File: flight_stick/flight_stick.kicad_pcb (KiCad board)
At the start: 2 copper layers, 75 x 50 mm, 61 parts, among them J10 USB_C_Receptacle_USB2.0, J11 Conn_01x05_Pin, J7 Conn_01x04_Male, J8 Conn_01x05_Pin, J9 Conn_ST_STDC14, Q4 2N7002, Q5 2N7002, Q6 2N7002, Q7 2N7002, Q8 2N7002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

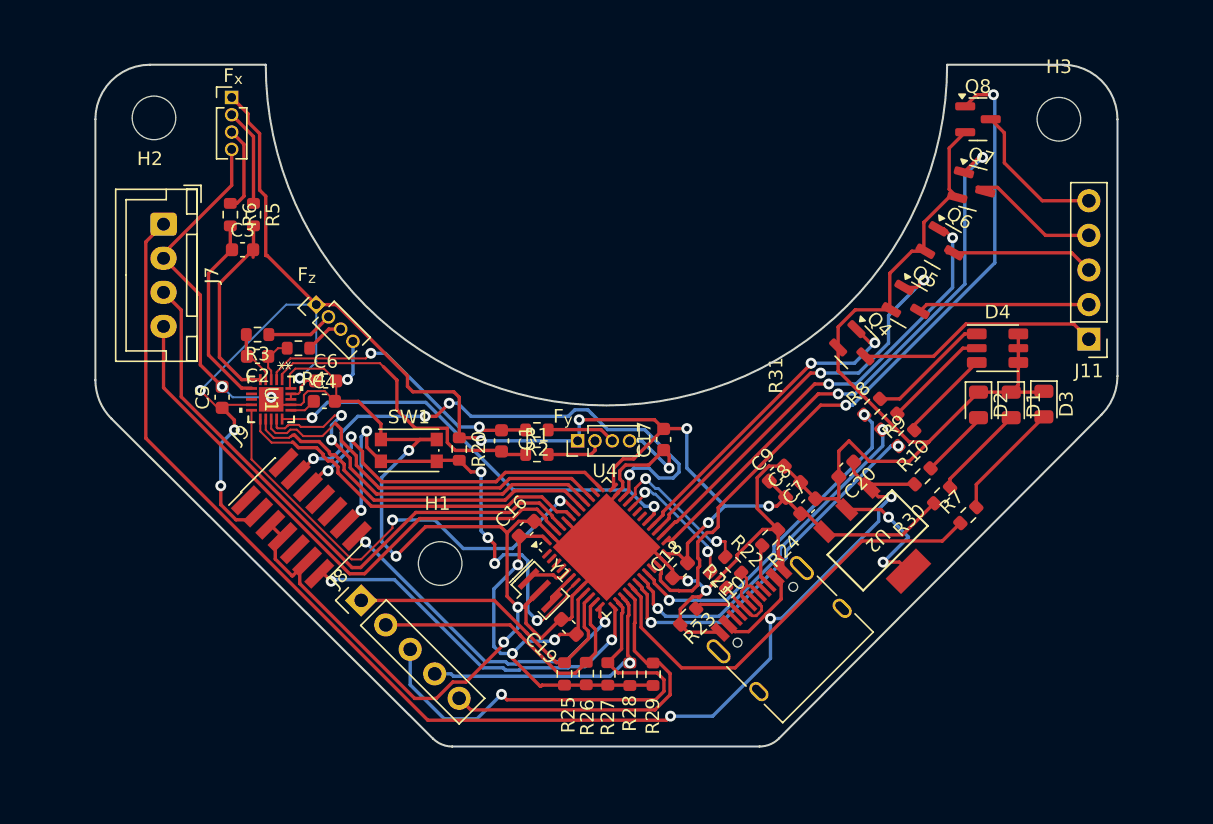
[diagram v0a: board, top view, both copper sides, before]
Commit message: Touchups
- Added GND pour on top
- Cleaned up some traces
- Fixed 3V3 missing connections
- Reduced pad size on ADC for clearance
- Removed last vias in pads
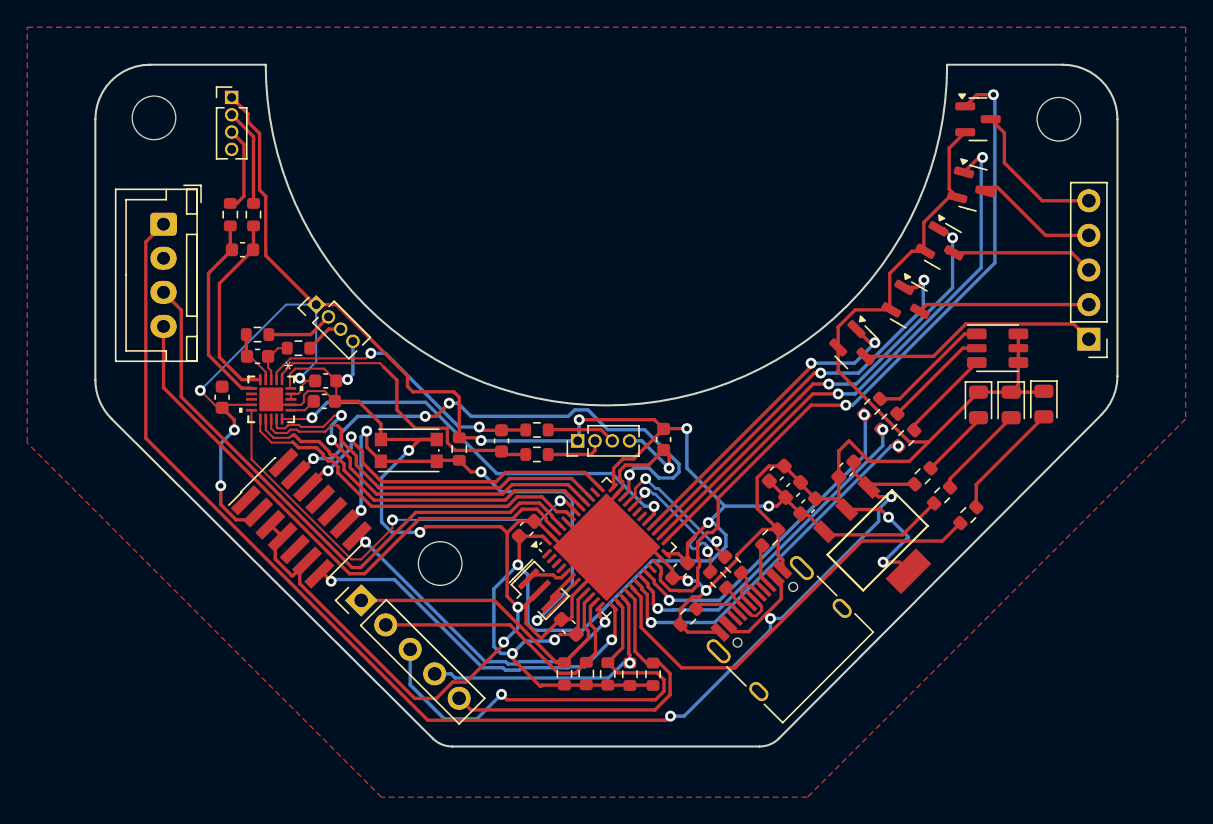
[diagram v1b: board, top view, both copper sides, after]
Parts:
- renumbered F_{y} to J1, F_{z} to J3, F_{x} to J5
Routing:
- net GND: track 261.4 -> 234.0 mm, vias 12 -> 10
- net +3.3V: track 162.4 -> 186.8 mm
- net /mcureset: track 36.9 -> 39.6 mm, vias 6 -> 4
- net /ADC_CS: track 34.6 -> 32.9 mm
- net /D-: track 9.79 -> 11.1 mm
- net +5V: track 103.6 -> 102.4 mm
- net /StatusLED_{B}: track 25.2 -> 24.5 mm
- net /StatusLED_{R}: track 26.1 -> 25.5 mm
- net Net-(U1-AIN2P): track 14.9 -> 14.3 mm
- added copper zone on F.Cu, net GND

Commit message: Updated Layout, Added Assembly part #s
Cleaned up layout for assembly minimum spacing

Added JLCPCB part #s for preorder and manufacturing
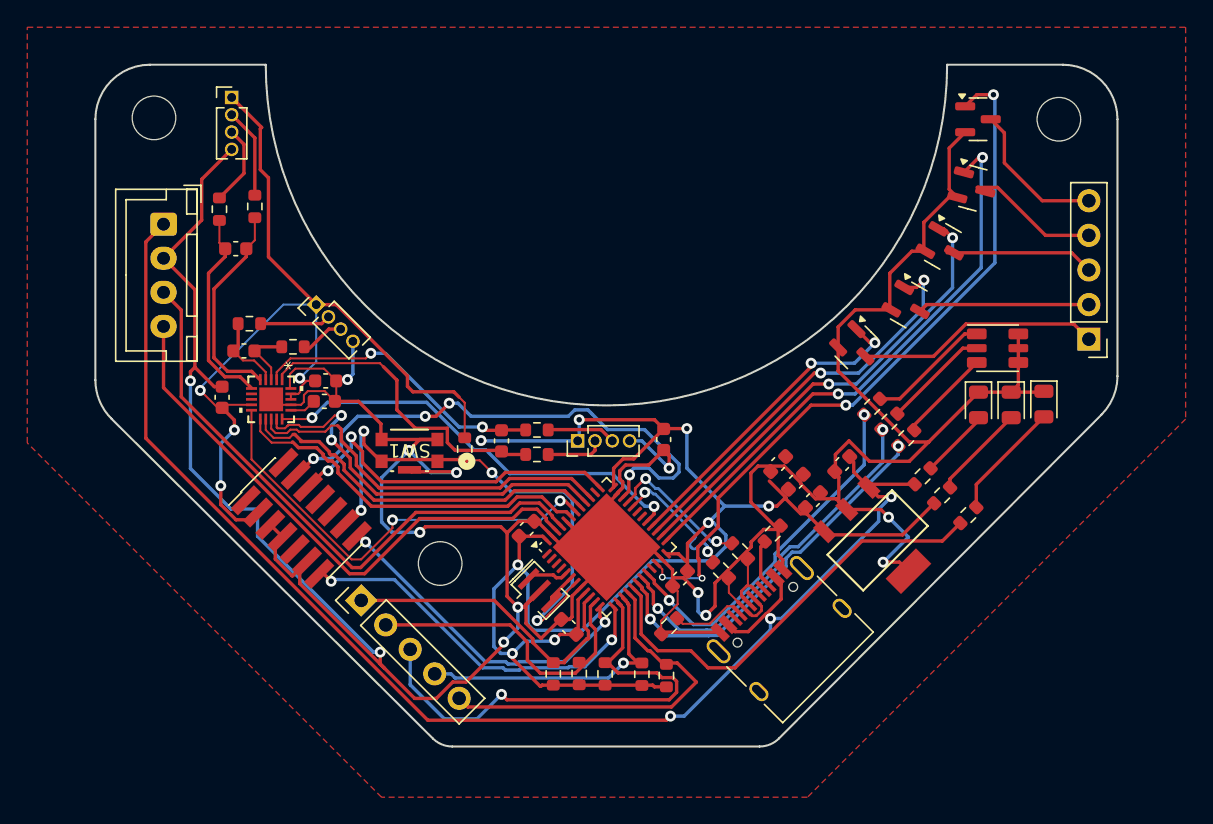
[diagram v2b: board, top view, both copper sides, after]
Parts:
- C1: value 100nF -> 100n
- C20: value 0.47uF -> 470n
- SW1: value SW_Push -> KMR223G LFG; footprint Button_Switch_SMD:SW_Push_1P1T_NO_CK_KMR2 -> flight_stick_footprints:KMR2_G_CNK
- moved R23 1.57 mm to (152.1, 146.2)
- moved R22 1.12 mm to (157.3, 140.7)
- moved C2 1.08 mm to (120.9, 126.0)
- moved R3 1.00 mm to (121.3, 124.0)
- moved R29 0.99 mm to (151.9, 149.8)
- moved R6 0.89 mm to (119.1, 115.6)
- moved R28 0.88 mm to (150.1, 149.7)
- moved R25 0.82 mm to (143.6, 149.7)
- moved R21 0.73 mm to (155.9, 142.1)
- moved C9 0.71 mm to (160.1, 134.3)
- moved C8 0.63 mm to (161.4, 135.6)
- moved R5 0.61 mm to (121.7, 115.4)
- moved C18 0.60 mm to (152.9, 142.7)
- moved C7 0.57 mm to (162.7, 136.9)
- moved R26 0.52 mm to (145.5, 149.7)
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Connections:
- SW1 pad 1: GND -> /mcureset
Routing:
- net GND: track 234.0 -> 299.0 mm, vias 10 -> 13
- net /StatusLED_{R}: track 25.5 -> 27.7 mm
- net /button5: track 25.7 -> 27.8 mm
- net /StatusLED_{B}: track 24.5 -> 26.6 mm
- net Net-(J10-CC1): track 3.56 -> 5.48 mm
- net /button3: track 34.0 -> 35.8 mm
- net Net-(U1-AIN1P): track 4.03 -> 5.72 mm
- net /button4: track 20.0 -> 21.4 mm
- net /StatusLED_{G}: track 26.8 -> 28.2 mm
- net Net-(U1-AIN1N): track 3.45 -> 4.74 mm
- net Net-(U1-AIN2P): track 14.3 -> 15.6 mm
- net /Trans5: track 54.2 -> 53.0 mm, vias 2 -> 4
- net /d+: track 4.02 -> 4.89 mm
- net /button2: track 21.5 -> 22.3 mm
- net /D-: track 11.1 -> 10.5 mm
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
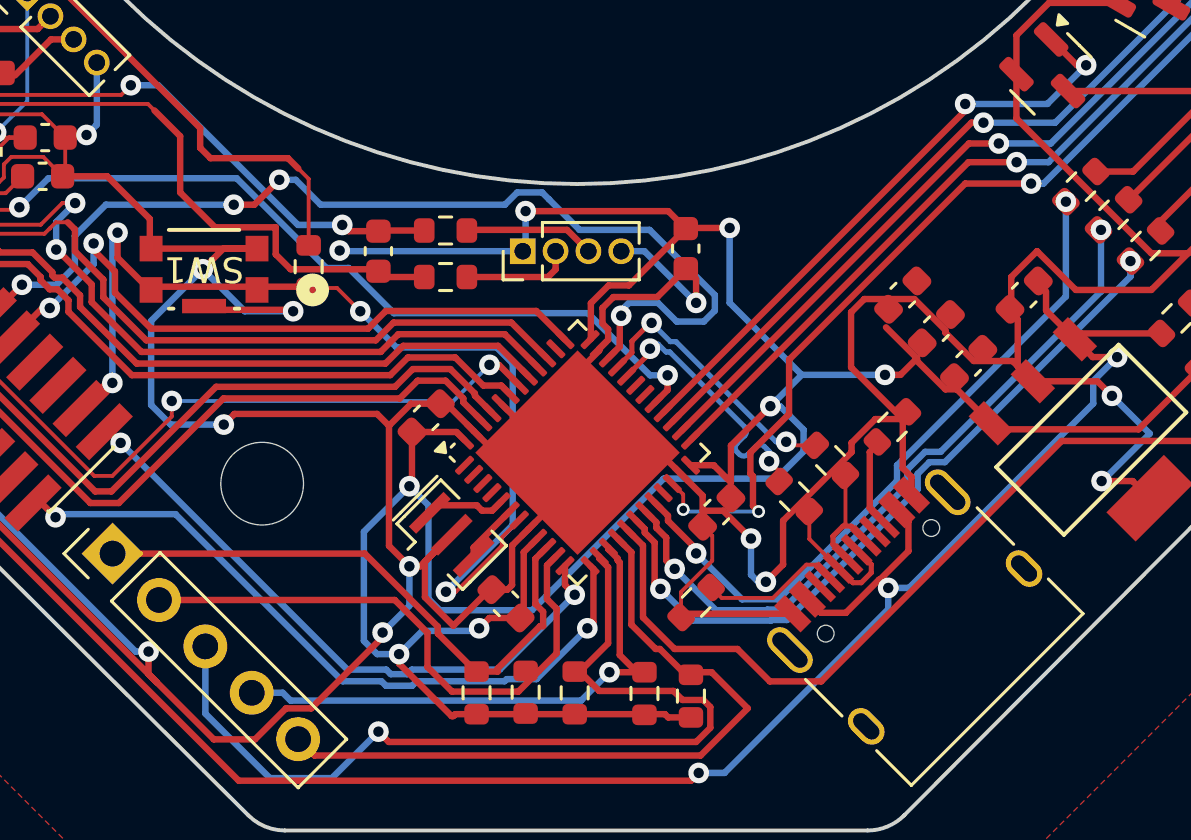
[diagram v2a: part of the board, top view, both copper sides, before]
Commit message: Ammended DRC Violations
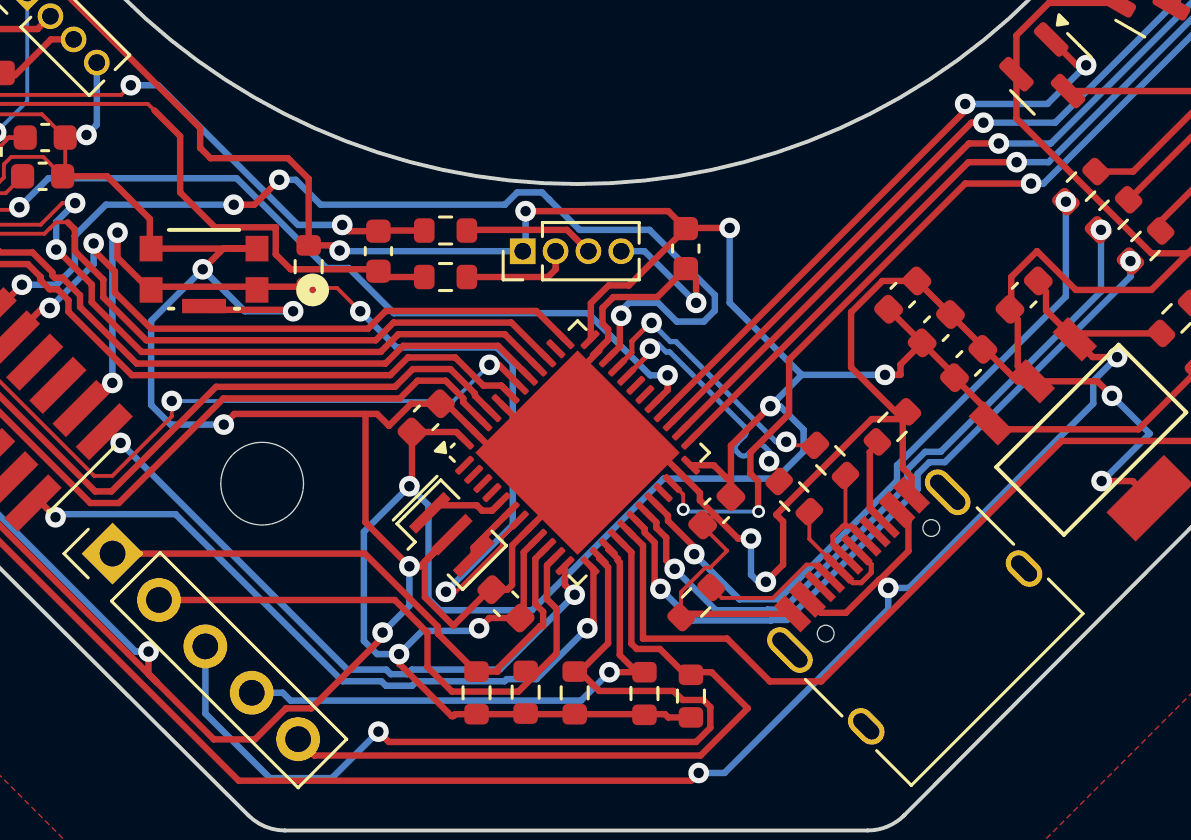
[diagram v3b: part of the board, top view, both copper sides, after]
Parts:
- moved C18 0.05 mm to (152.9, 142.6)
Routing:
- net GND: track 299.0 -> 301.7 mm
- net +3.3V: track 186.7 -> 189.3 mm

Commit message: FINISHED AND ORDERED DAT HOE
REV 4 COMPLETED, GERBER FILES PRODUCED, ASSEMBLY SUBMITTED
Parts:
- moved Q6 0.99 mm to (173.0, 118.9)
- moved Q7 0.92 mm to (175.2, 114.5)
- moved Q5 0.84 mm to (170.3, 123.2)
- moved J5 0.78 mm to (119.4, 106.9)
- moved Q4 0.75 mm to (166.4, 126.2)
- moved Q8 0.74 mm to (175.5, 109.1)
- moved C1 0.53 mm to (139.7, 133.1)
- moved R1 0.40 mm to (142.4, 134.0)
- moved R2 0.40 mm to (142.4, 132.2)
- moved J1 0.30 mm to (145.4, 132.9)
- moved C17 0.22 mm to (151.8, 132.7)
- moved J3 0.14 mm to (126.1, 122.7)
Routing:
- net Net-(J1-Pin_3): track 5.06 -> 7.17 mm, vias 0 -> 2
- net /Trans3: track 33.9 -> 36.0 mm
- net Net-(J11-Pin_4): track 9.66 -> 7.94 mm
- net Net-(J11-Pin_3): track 10.9 -> 9.85 mm
- net /Trans5: track 53.0 -> 53.9 mm
- net /Trans2: track 30.1 -> 29.3 mm
- net Net-(J5-Pin_2): track 6.61 -> 7.36 mm
- net +3.3V: track 189.3 -> 190.1 mm, vias 12 -> 11
- net Net-(J1-Pin_2): track 4.26 -> 4.79 mm
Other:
- outline, holes or cut-outs redrawn
- board text added: "+"
- board text added: "-"
- board text added: "1 2 3 4 5"
- board text added: "3V3"
- board text added: "5 4 3 2 1"
- board text added: "5V"
- board text added: "A+"
- board text added: "A-"
- board text added: "Aryan Ghosh ^_^"
- board text added: "CL"
- board text added: "DA"
- board text added: "University of Toronto Human Powered Vehicles Design Team"
